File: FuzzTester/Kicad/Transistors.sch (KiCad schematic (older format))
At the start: 34 parts, among them Q1 PN2222A, Q10 2SC1815, Q11 S8050, Q12 S9013, Q13 S9014, Q14 S9018, Q15 BC848B, Q16 2SC1623, Q17 MPSA18, Q18 MPSA18, Q19 2N5088, Q2 MMBT3904, Q20 2N5088, Q3 MMBT5551L, Q4 MMBTA42, Q5 BC807, Q6 BC846, Q7 BC847B, Q8 BC847C, Q9 C945, U10 CD4052B, U11 CD4052B, U12 CD4052B, U6 CD4052B, U7 CD4051B, U8 CD4052B, U9 CD4051B

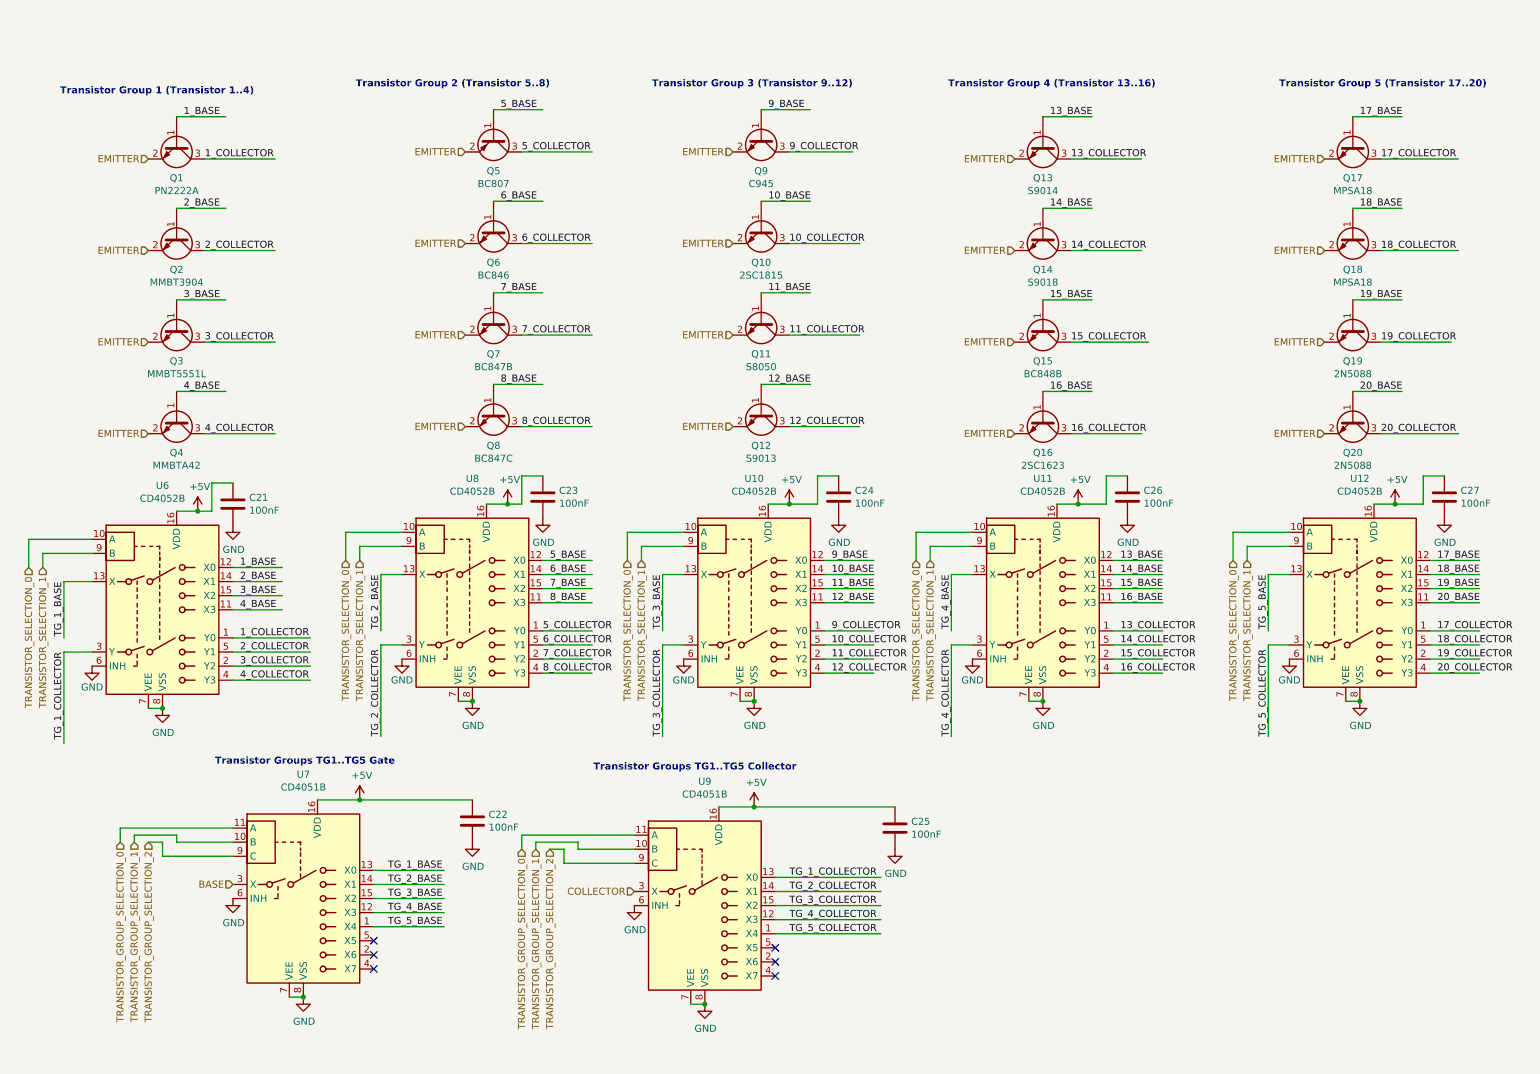
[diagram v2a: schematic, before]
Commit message: Power regulator -9V
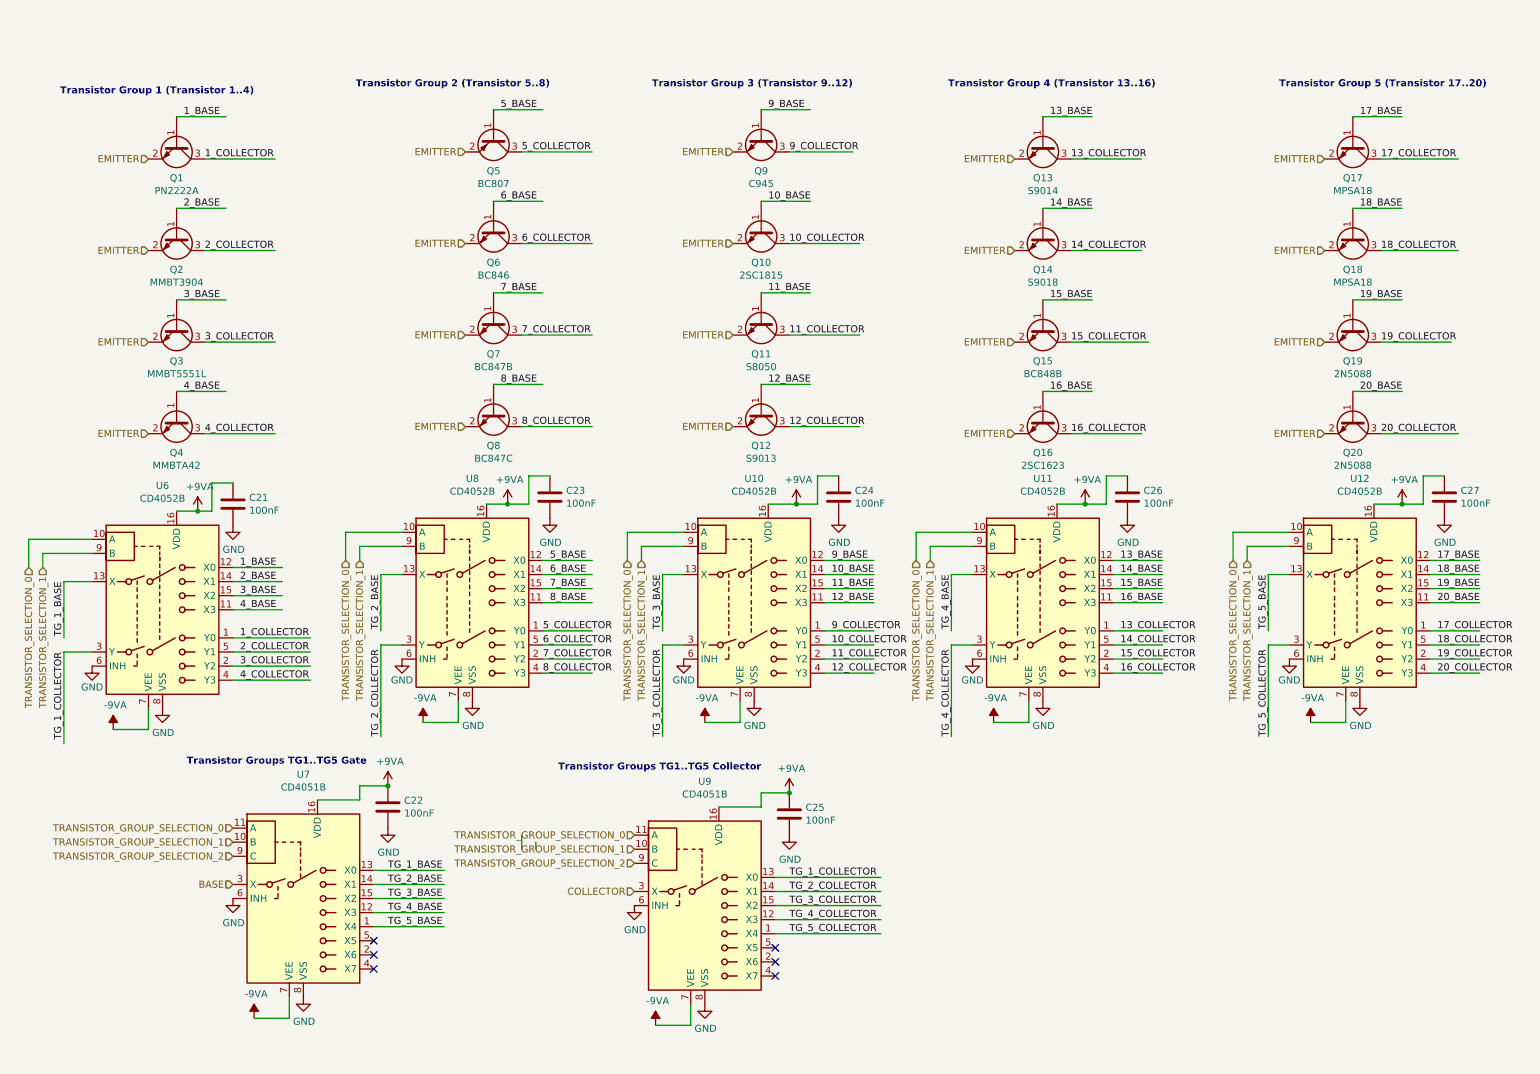
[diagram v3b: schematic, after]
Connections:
- net labels added: +9VA, -9VA
- net labels removed: +5V
- wire segments 179 -> 172
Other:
- moved on the sheet: C22, C23, C25

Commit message: PCB Placement 100x82
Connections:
- net labels added: +9V
- net labels removed: +9VA, -9VA
- wire segments 172 -> 165
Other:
- moved on the sheet: C32, C33, Q33, Q34, Q35, Q36, U16, U18
